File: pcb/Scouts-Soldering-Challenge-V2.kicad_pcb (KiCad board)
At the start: 2 copper layers, 76.2 x 78.7 mm, 13 parts, among them J1 Barrel_Jack, SW1 SW_Push

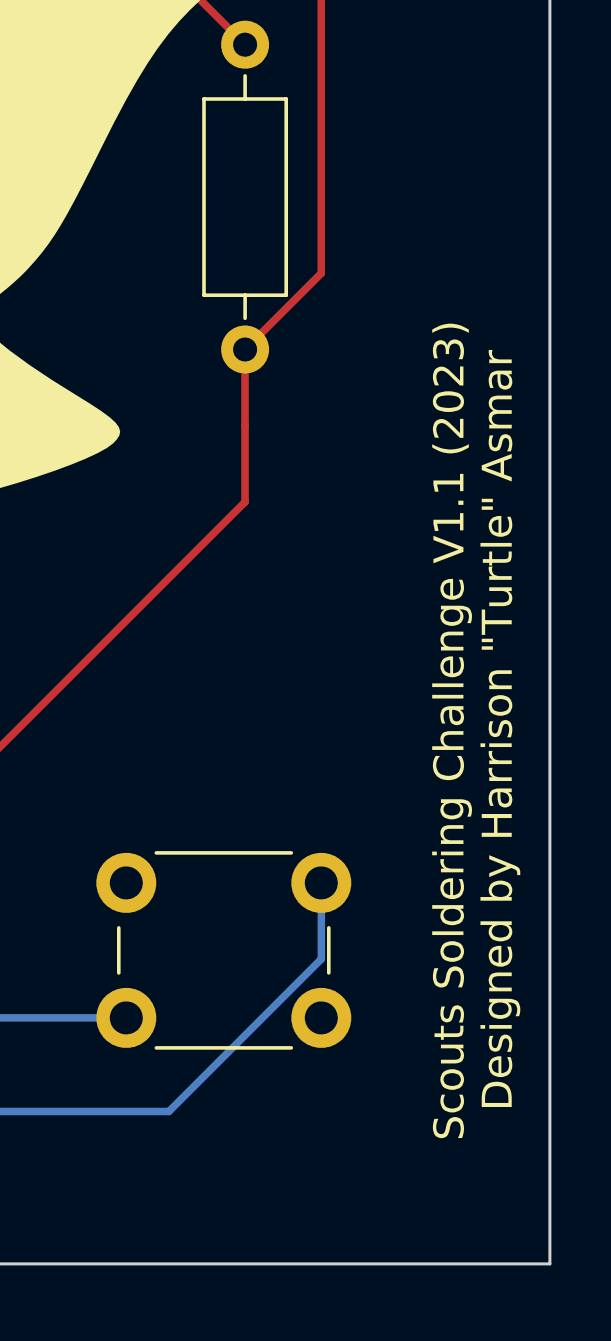
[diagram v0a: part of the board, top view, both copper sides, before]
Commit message: Silkscreen version update to V2.0
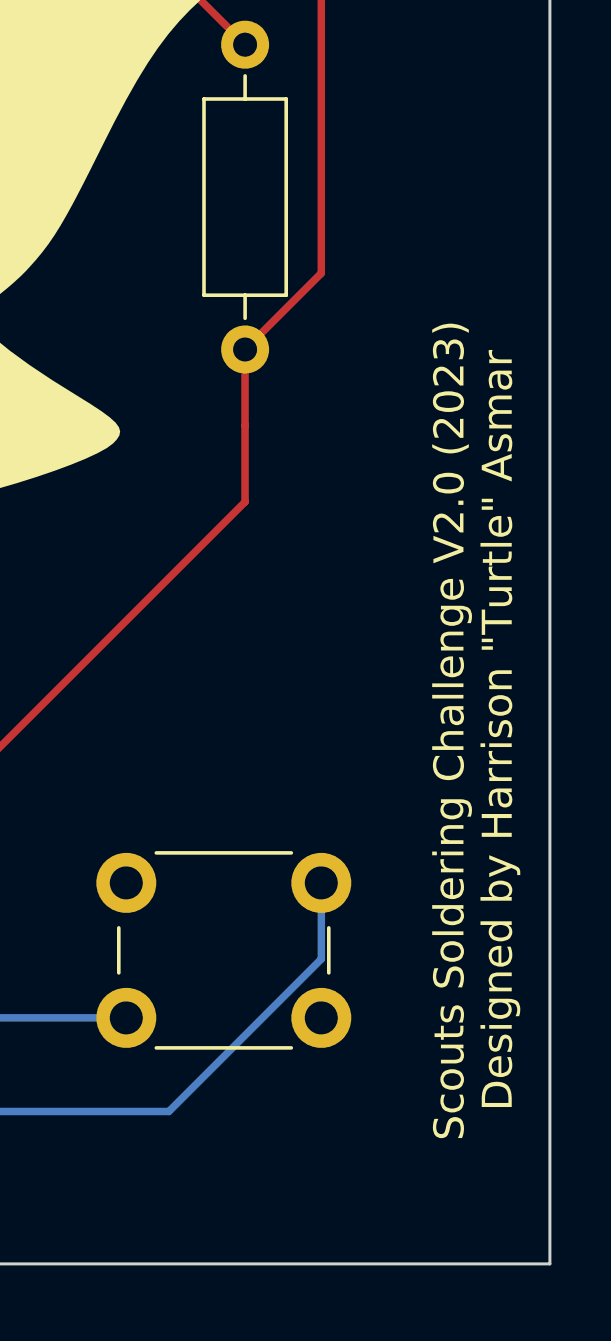
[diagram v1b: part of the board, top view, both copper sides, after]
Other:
- board text added: "Scouts Soldering Challenge V2.0 (2023) Designed by Harrison {dblquote}Turtle{dblquote} Asmar"
- board text removed: "Scouts Soldering Challenge V1.1 (2023) Designed by Harrison {dblquote}Turtle{dblquote} Asmar"
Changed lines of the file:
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@@
     (effects (font (size 1.5 1.5) (thickness 0.3) bold) (justify left bottom mirror))
   )
-  (gr_text "Scouts Soldering Challenge V1.1 (2023)\nDesigned by Harrison {dblquote}Turtle{dblquote} Asmar" (at 190.5 109.22 90) (layer "F.SilkS")
+  (gr_text "Scouts Soldering Challenge V2.0 (2023)\nDesigned by Harrison {dblquote}Turtle{dblquote} Asmar" (at 190.5 109.22 90) (layer "F.SilkS")
     (effects (font (size 1 1) (thickness 0.15)))
   )

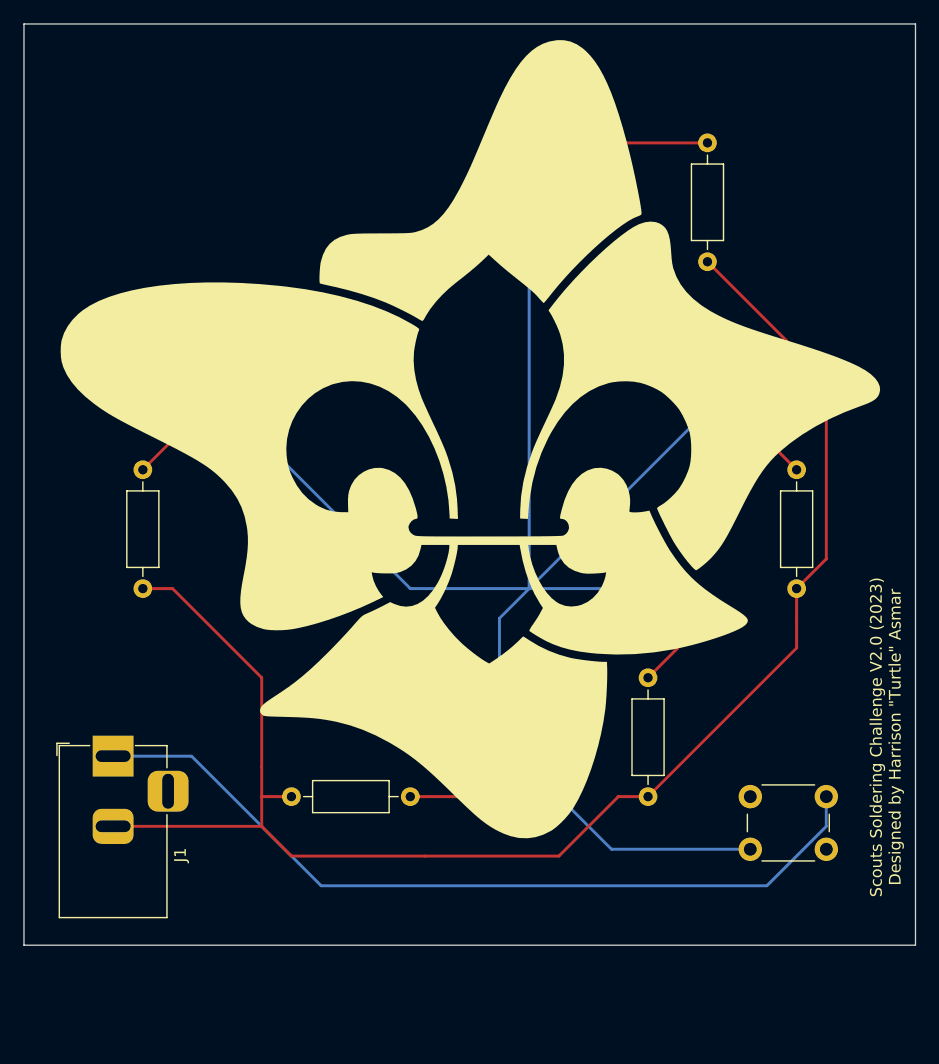
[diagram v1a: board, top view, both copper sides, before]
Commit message: V2.1 of PCB and Schematic
Complete overhall, adds a buzzer, replaces the barrel jack with a battery and changes the resistors to match. Also moves things around a lot.
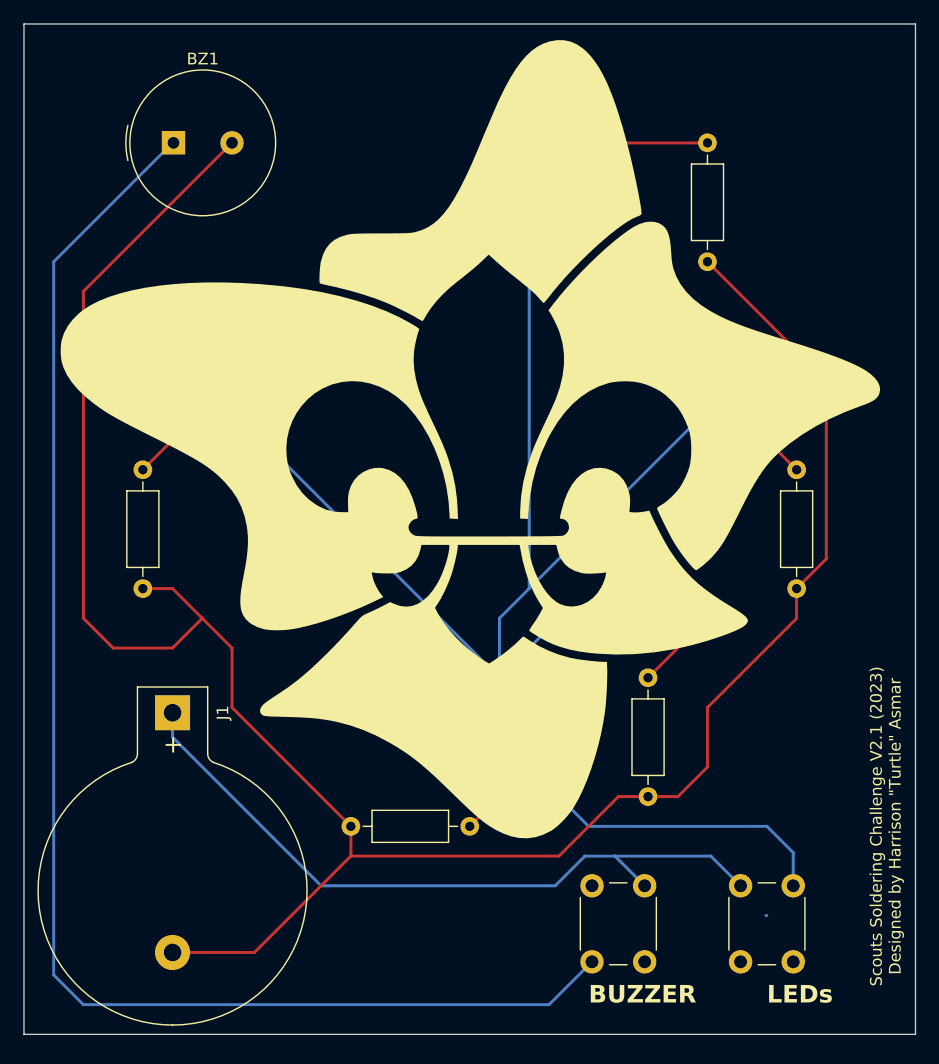
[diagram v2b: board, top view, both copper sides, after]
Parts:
- added BZ1: Buzzer, Buzzer_Beeper:Buzzer_TDK_PS1240P02BT_D12.2mm_H6.5mm, F.Cu at (129.6, 58.4)
- added SW2: SW_Push, Button_Switch_THT:SW_PUSH_6mm, F.Cu at (169.9, 121.9)
- J1: value Barrel_Jack -> Coin_Battery; footprint Connector_BarrelJack:BarrelJack_Horizontal -> Battery:BatteryHolder_Keystone_103_1x20mm
- R1, R2, R3, R4, R5: value 330R -> 51R
- moved SW1 8.46 mm to (182.6, 121.9), turned to -90 degrees
- moved J1 6.29 mm to (129.5, 107.1), turned to -90 degrees
- moved R3 5.68 mm to (154.9, 116.8)
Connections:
- J1 pad 1: Net-(J1-Pad1) -> Net-(J1-+)
- SW1 pad 1: Net-(J1-Pad1) -> Net-(D1-A)
- SW1 pad 2: Net-(D1-A) -> Net-(J1-+)
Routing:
- net Net-(BZ1--): track 0.00 -> 124.3 mm
- net Net-(J1-Pad1): track 70.2 -> 0.00 mm
- net Net-(J1-+): track 0.00 -> 61.6 mm
- net Net-(BZ1-+): track 133.7 -> 193.8 mm
- net Net-(D1-A): track 152.5 -> 170.0 mm
- net Net-(D2-K): track 15.2 -> 11.2 mm
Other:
- board size 76.2 x 78.7 mm -> 76.2 x 86.4 mm
- board text added: "51R"
- board text added: "BUZZER"
- board text added: "LEDs"
- board text added: "Scouts Soldering Challenge V2.1 (2023) Designed by Harrison {dblquote}Turtle{dblquote} Asmar"
- board text removed: "300R"
- board text removed: "330R"
- board text removed: "Scouts Soldering Challenge V2.0 (2023) Designed by Harrison {dblquote}Turtle{dblquote} Asmar"
